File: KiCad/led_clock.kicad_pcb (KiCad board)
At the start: 2 copper layers, 100 x 100 mm, 71 parts, among them P1 5V, SW1 SECONDS, SW2 MINUTES, SW3 HOURS, U1 74HCT4060, U10 74LS47, U11 74LS90, U12 74LS90, U13 74LS90, U14 74LS90, U15 74LS90, U16 74LS90, U2 74LS00, U3 74LS00, U4 74LS00, U5 74LS47, U6 74LS47, U7 74LS47, U8 74LS47, U9 74LS47, X1 32768Hz

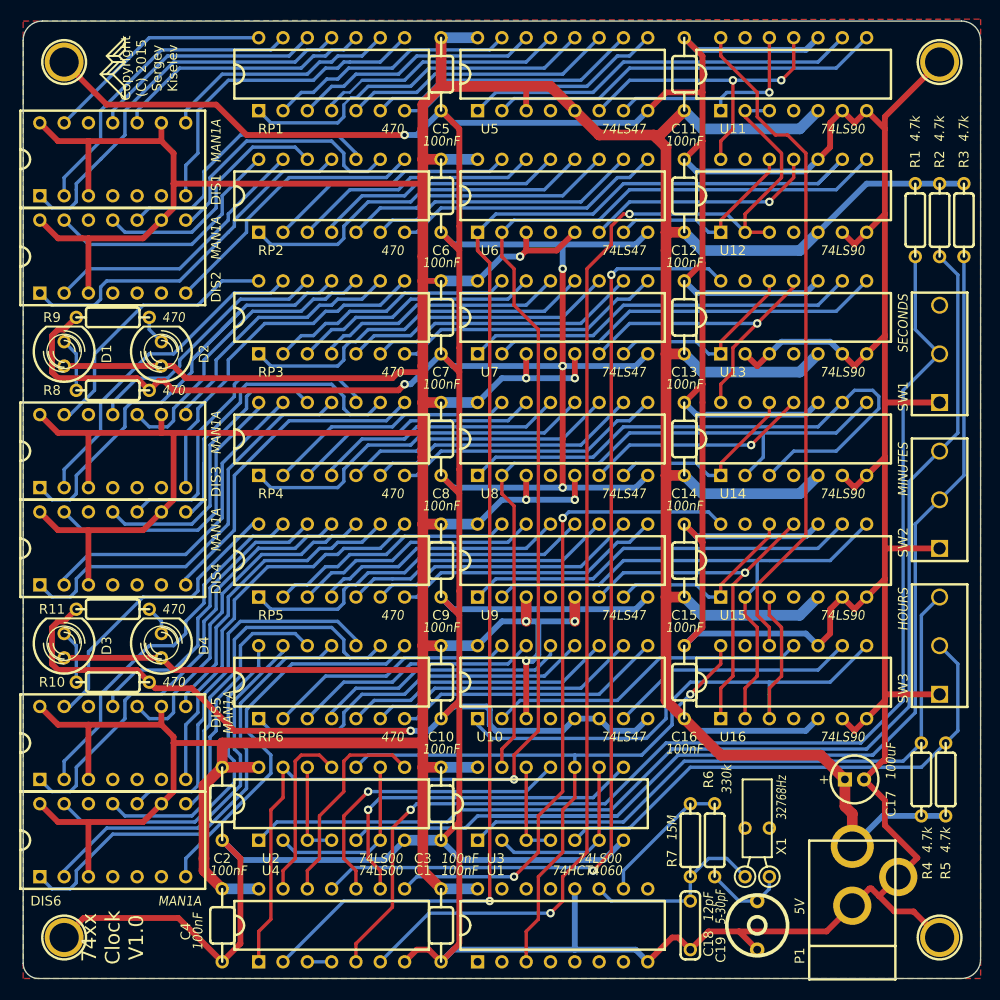
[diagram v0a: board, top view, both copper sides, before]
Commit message: Add files for version 1.1
Signed-off-by: Sergey Kiselev <skiselev@gmail.com>
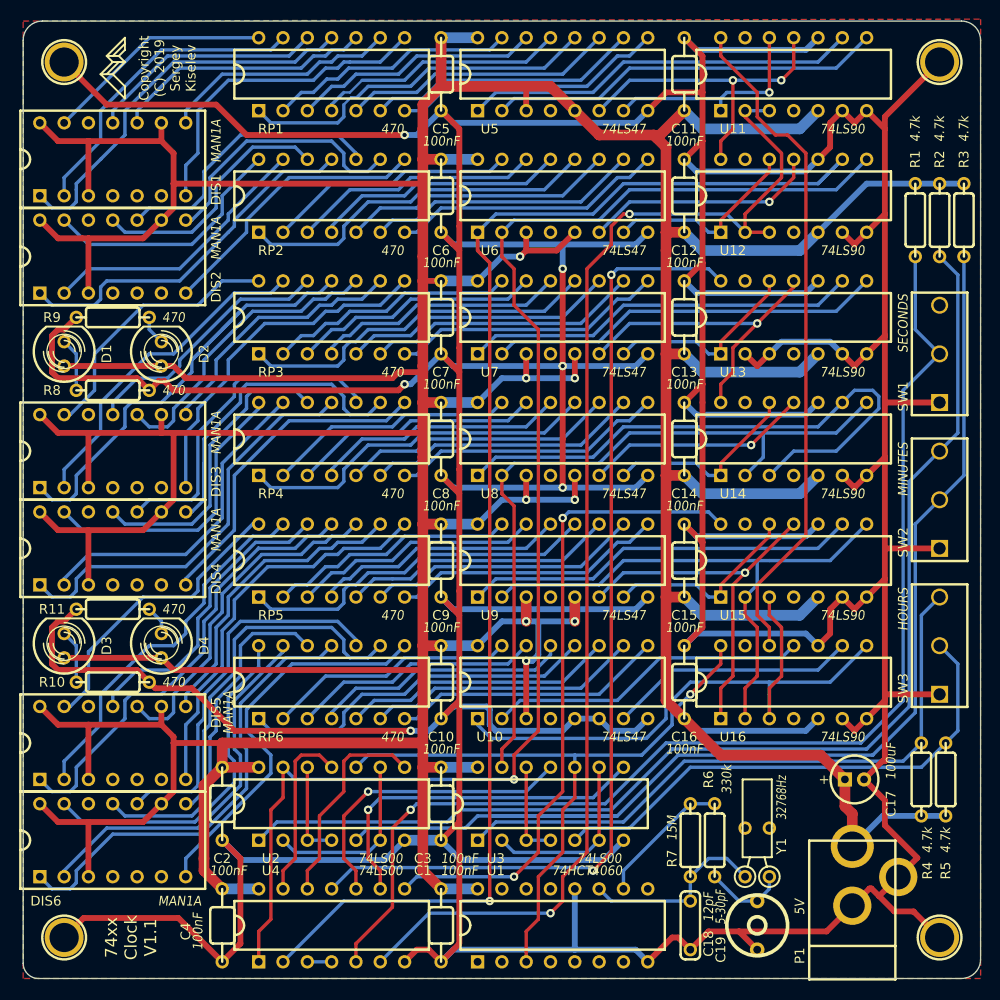
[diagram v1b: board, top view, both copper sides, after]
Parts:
- renumbered X1 to Y1
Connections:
- DIS1 pad 6: (no net) -> Net-(DIS1-Pad6)
- DIS2 pad 6: (no net) -> Net-(DIS2-Pad6)
- DIS3 pad 6: (no net) -> Net-(DIS3-Pad6)
- DIS4 pad 6: (no net) -> Net-(DIS4-Pad6)
- DIS5 pad 6: (no net) -> Net-(DIS5-Pad6)
- DIS6 pad 6: (no net) -> Net-(DIS6-Pad6)
- SW1 pad 3: (no net) -> Net-(SW1-Pad3)
- U1 pad 1: (no net) -> Net-(U1-Pad1)
- U1 pad 13: (no net) -> Net-(U1-Pad13)
- U1 pad 14: (no net) -> Net-(U1-Pad14)
- U1 pad 15: (no net) -> Net-(U1-Pad15)
- U1 pad 2: (no net) -> Net-(U1-Pad2)
- U1 pad 4: (no net) -> Net-(U1-Pad4)
- U1 pad 5: (no net) -> Net-(U1-Pad5)
- U1 pad 6: (no net) -> Net-(U1-Pad6)
- U1 pad 7: (no net) -> Net-(U1-Pad7)
- U1 pad 9: (no net) -> Net-(U1-Pad9)
- U10 pad 4: (no net) -> Net-(U10-Pad4)
- U5 pad 4: (no net) -> Net-(U5-Pad4)
- U6 pad 4: (no net) -> Net-(U6-Pad4)
- U7 pad 4: (no net) -> Net-(U7-Pad4)
- U8 pad 4: (no net) -> Net-(U8-Pad4)
- U9 pad 4: (no net) -> Net-(U9-Pad4)
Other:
- board text added: "74xx Clock V1.1"
- board text added: "Copyright (C) 2019 Sergey Kiselev"
- board text removed: "74xx Clock V1.0"
- board text removed: "Copyright (C) 2015 Sergey Kiselev"
